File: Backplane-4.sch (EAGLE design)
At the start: 6 parts, among them X1 FAC64SNO_DRILL, X2 FAC64SNO_DRILL, X3 FAC64SNO_DRILL, X4 FAC64SNO_DRILL

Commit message: Schaltpläne aufgehübscht zur Veröffentlichung
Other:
- note added: "HomePi - Backplane Rev. 2019/05"

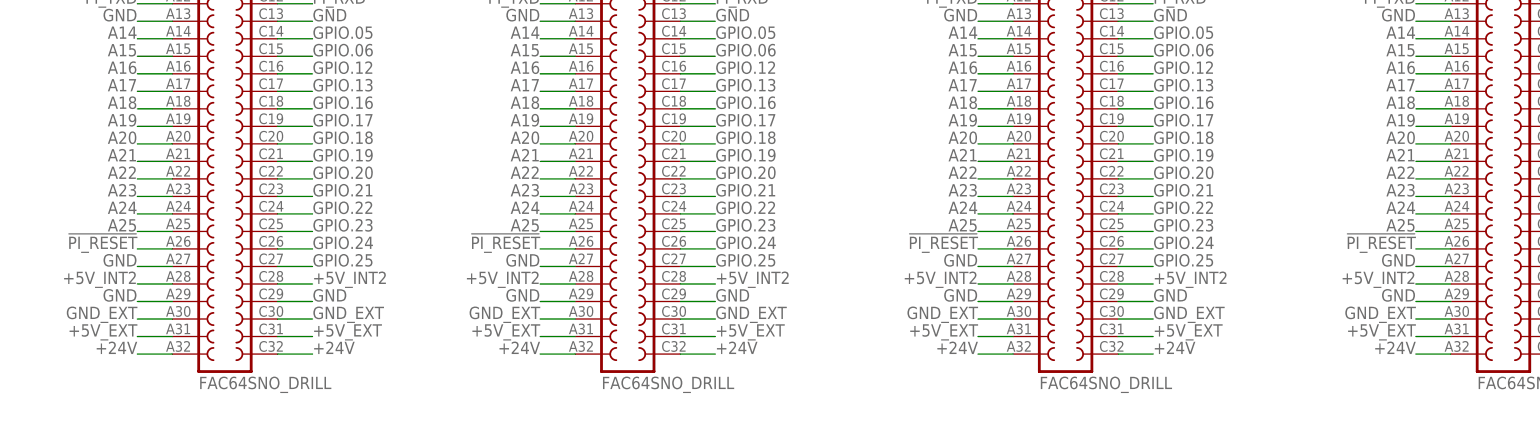
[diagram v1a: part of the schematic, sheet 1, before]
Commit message: Verbesserte Stromversorgung, Pi-Kühler, CAN-Bus 8x-Schalter
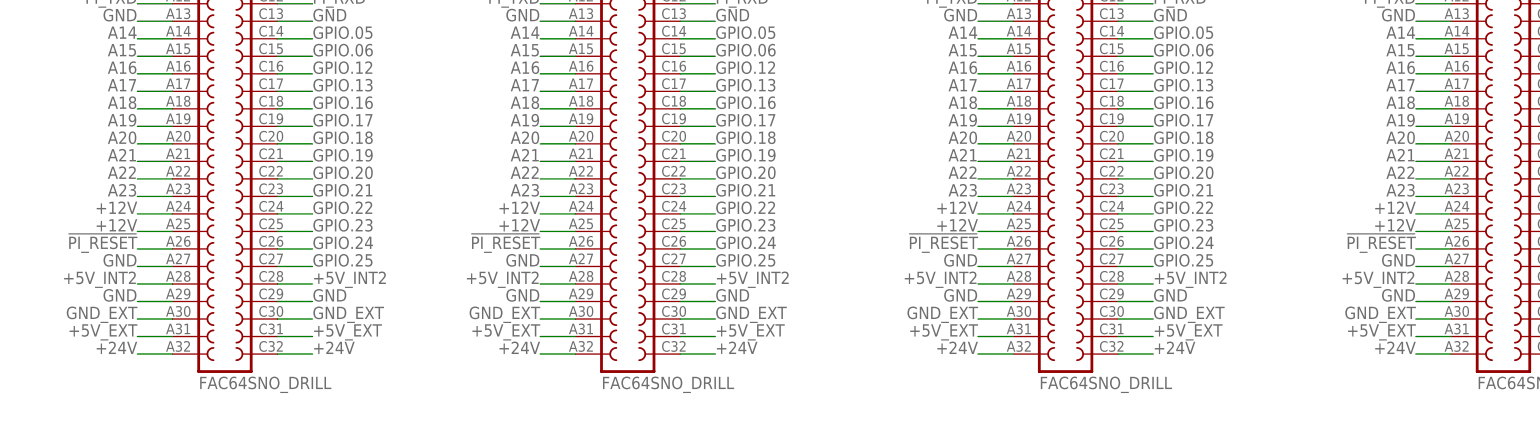
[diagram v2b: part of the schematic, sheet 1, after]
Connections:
- removed net A24: SV1.47, SV2.47, X1.A24, X2.A24, X3.A24, X4.A24
- removed net A25: SV1.49, SV2.49, X1.A25, X2.A25, X3.A25, X4.A25
- new net +12V: SV1.47, SV1.49, SV2.47, SV2.49, X1.A24, X1.A25, X2.A24, X2.A25, X3.A24, X3.A25, X4.A24, X4.A25
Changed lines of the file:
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@@
 </segment>
 </net>
-<net name="A24" class="0">
+<net name="+12V" class="0">
 <segment>
 <pinref part="X1" gate="G$1" pin="A24"/>
@@
 <pinref part="X4" gate="G$1" pin="A24"/>
 </segment>
-</net>
-<net name="A25" class="0">
 <segment>
 <pinref part="X1" gate="G$1" pin="A25"/>
@@
 </segment>
 </net>
-<net name="A24" class="0">
+<net name="+12V" class="0">
 <segment>
 <wire x1="33.02" y1="86.36" x2="27.94" y2="86.36" width="0.1524" layer="91"/>
@@
 <pinref part="SV2" gate="1" pin="47"/>
 </segment>
-</net>
-<net name="A25" class="0">
 <segment>
 <wire x1="33.02" y1="83.82" x2="27.94" y2="83.82" width="0.1524" layer="91"/>
